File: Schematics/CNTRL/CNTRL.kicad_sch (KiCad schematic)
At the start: 128 parts, among them J1 SWD, J10 Y+, J11 Y-, J12 693071020811, J13 3.3V, J14 NAV I2C, J15 I2C, J16 USART, J17 PYRO1_OSTTE020104, J18 PYRO3_OSTTE020104, J19 USB_A_TE_292303-7_Horizontal, J2 CONSMA001-SMD-G-T, J20 PYRO2_OSTTE020104, J21 PYRO4_OSTTE020104, J3 3S LiPo, J4 F4, J5 F3, J6 F2, J7 F1, J8 X+, J9 X-, Q1 BUK9832-55A_CUX, Q2 BUK9832-55A_CUX, Q3 BUK9832-55A_CUX, Q4 BUK9832-55A_CUX, Q5 MMBT2222A-TP, SW1 OS102011MS2QN1, SW2 Omron_B3F-10xx, U1 STM32405RGT6, U2 RFM95W-915S2, U3 TPS2117DRLR, U4 TPS563200, U5 AMS1117-3.3, U6 AMS1117-5.0, U7 W25Q128JVSIQ, U8 USBLC6-2SC6, Y1 12MHz_ECS-120-18-33-JGN-TR3, Y2 32.768KHz_SC32S-7PF20PPM

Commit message: navig board pcb and schematic along with cntrl board edits
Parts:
- removed R11: 100K, Resistor_SMD:R_0603_1608Metric, symbol Device:R
- removed R22, R23, R36, R37: 10K, Resistor_SMD:R_0603_1608Metric, symbol Device:R
- removed R27, R28, R40, R41: 3.7K, Resistor_SMD:R_0603_1608Metric, symbol Device:R
- removed SW1: OS102011MS2QN1, External:SW_OS102011MS2QN1, symbol Switch:SW_SPDT
- added SW1: Omron_B3F-10xx, Button_Switch_THT:SW_TH_Tactile_Omron_B3F-10xx, symbol Switch:SW_Push
- J14: value NAV I2C -> NAVIG I2C
- R12: value 100K -> 10K
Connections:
- net +3.3V: now also SW1.2
- net BOOT0: now also SW1.1
- net GND: now also R1.2
- net PYRO_1_SENSE: no longer names the net of U1.9 (PC1)
- net PYRO_2_SENSE: no longer names the net of U1.11 (PC3)
- net PYRO_3_SENSE: no longer names the net of U1.26 (PB0)
- net PYRO_4_SENSE: no longer names the net of U1.28 (PB2)
- no-connect marks 10 -> 14

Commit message: NAVIG v1 fixes and some experimental CNTRL updates for v2
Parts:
- removed C24, C26: 10uF, Capacitor_SMD:C_0603_1608Metric, symbol Device:C
- removed Q5: MMBT2222A-TP, Package_TO_SOT_SMD:SOT-23, symbol Simulation_SPICE:NPN
- removed U6: AMS1117-5.0, Package_TO_SOT_SMD:SOT-223-3_TabPin2, symbol Regulator_Linear:AMS1117-5.0
- added Q5: BUK9832-55A_CUX, BUK9832-55A_CUX:TRANS_BUK9832-55A_CUX, symbol BUK9832-55A_CUX:BUK9832-55A_CUX
- added R11, R22, R23, R27, R36, R40, R42, R44: 10K, Resistor_SMD:R_0603_1608Metric, symbol Device:R
- added R28, R37, R41, R43: 68, Resistor_SMD:R_0603_1608Metric, symbol Device:R
- added U10, U11, U6, U9: TLP293GB-TPL_E, External:SO4_TOS, symbol TLP293:TLP293GB-TPL_E
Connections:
- net +3.3V: now also R11.2, R22.1, R23.2, R27.2, R28.2, R36.1, R37.2, R40.1, R41.2, R42.1, R43.2, R44.1
- net BUCK_+5V: now also C22.1, L2.2, R13.1
- net GND: now also Q5.3, U10.3, U11.3, U6.3, U9.3
- net SPI2_CSB: now also R22.2
- net SPI2_MISO: now also R27.1
- net SPI3_CSB: now also R11.1
- net SPI3_MISO: now also R23.1
- net at Q4.2, Q4.4, R30.1: now also U11.2
- net at Q3.2, Q3.4, R29.1: now also U9.2
- net at Q2.2, Q2.4, R19.1: now also U10.2
- net at Q1.2, Q1.4, R18.1: now also U6.2
- net at BZ1.2 (+): now also Q5.2, Q5.4
- net at R31.1: now also Q5.1
- net PYRO_2_SENSE: now reaches U1.11 (PC3)
- net PYRO_2_SENSE: now also R40.2, U9.4
- net PYRO_3_SENSE: now reaches U1.26 (PB0)
- net PYRO_3_SENSE: now also R44.2, U10.4
- net PYRO_4_SENSE: now reaches U1.28 (PB2)
- net PYRO_4_SENSE: now also R42.2, U11.4
- net PYRO_1_SENSE: now reaches U1.9 (PC1)
- net PYRO_1_SENSE: now also R36.2, U6.4
- new net: R28.1, U6.1
- new net: R37.1, U9.1
- new net: R41.1, U11.1
- new net: R43.1, U10.1
- no-connect marks 14 -> 10
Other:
- moved on the sheet: J17, J18, J20, J21, Q1, Q2, Q3, Q4, R18, R19, R20, R21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

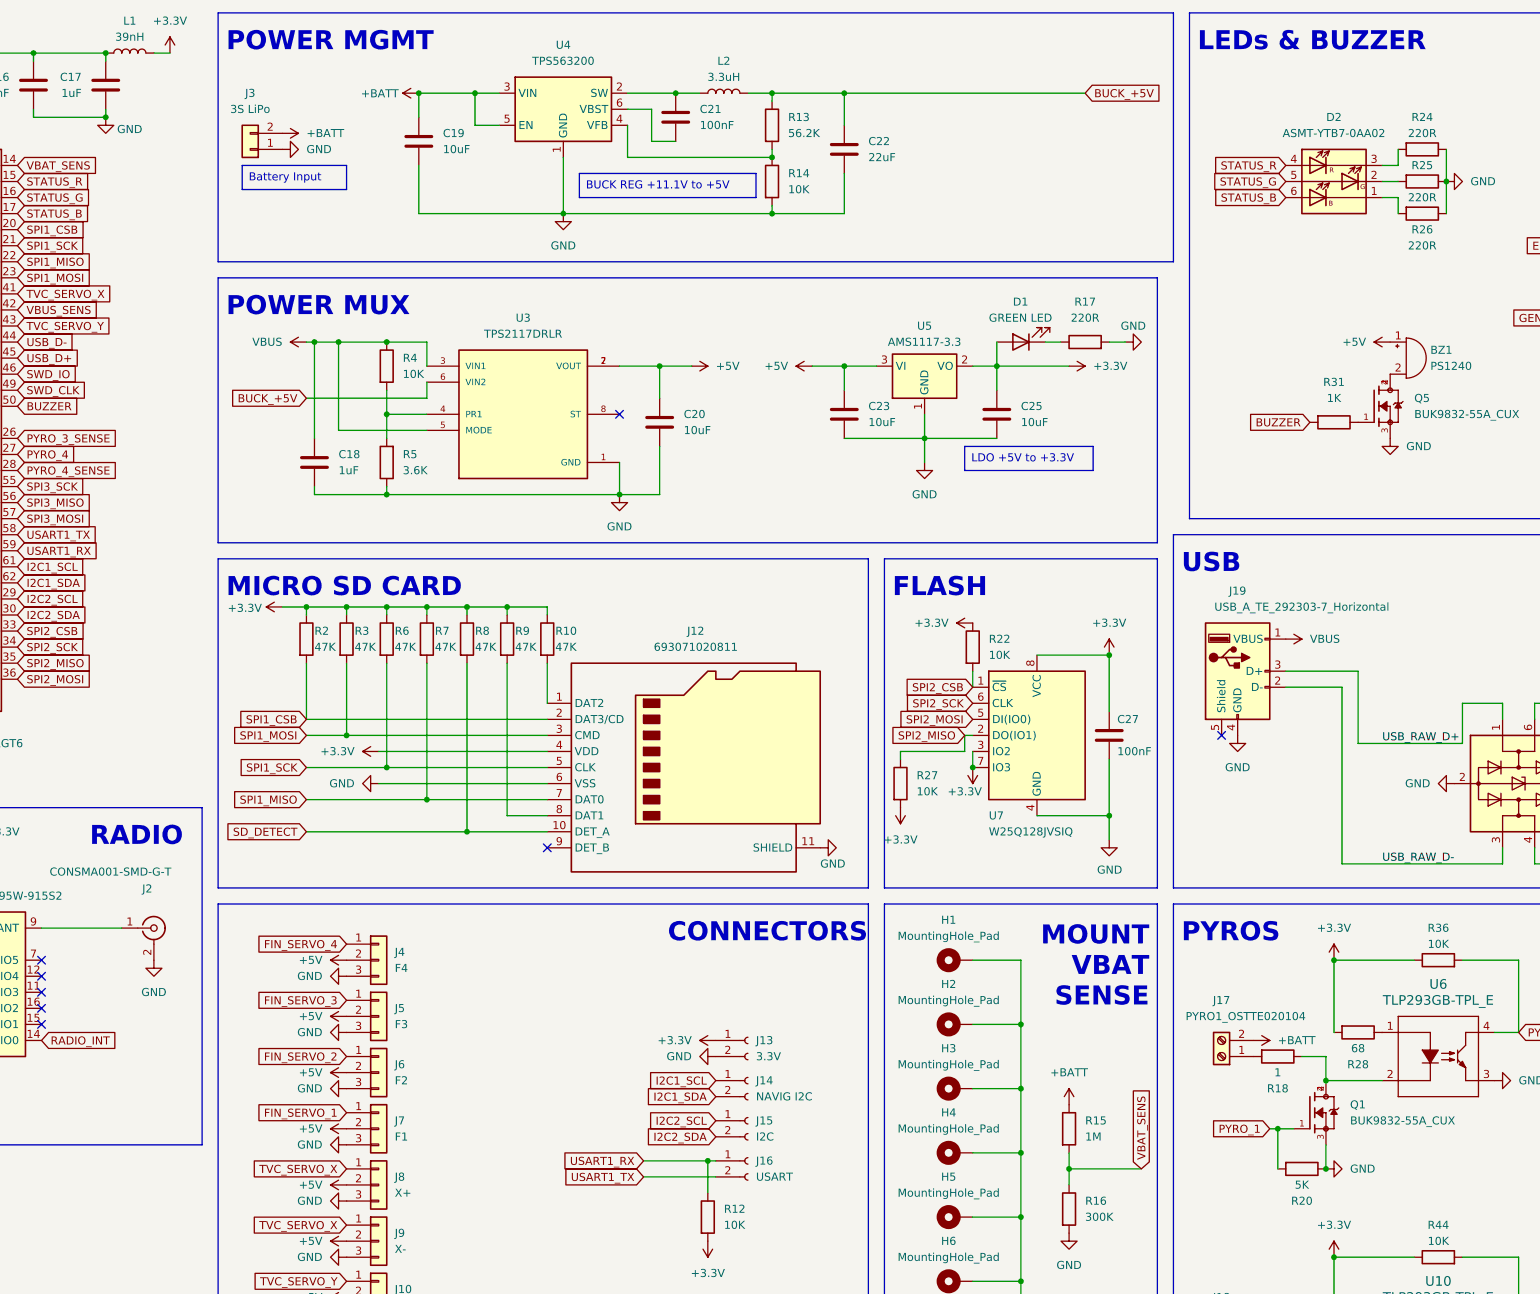
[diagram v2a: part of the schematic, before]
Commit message: initial coding/integration
i2c slave done (kinda doesnt work)
bno055 done (untested)
bmp390 done (untested)
neom9n not done
w25q128jv done (untested)
sd card/fatfs not done
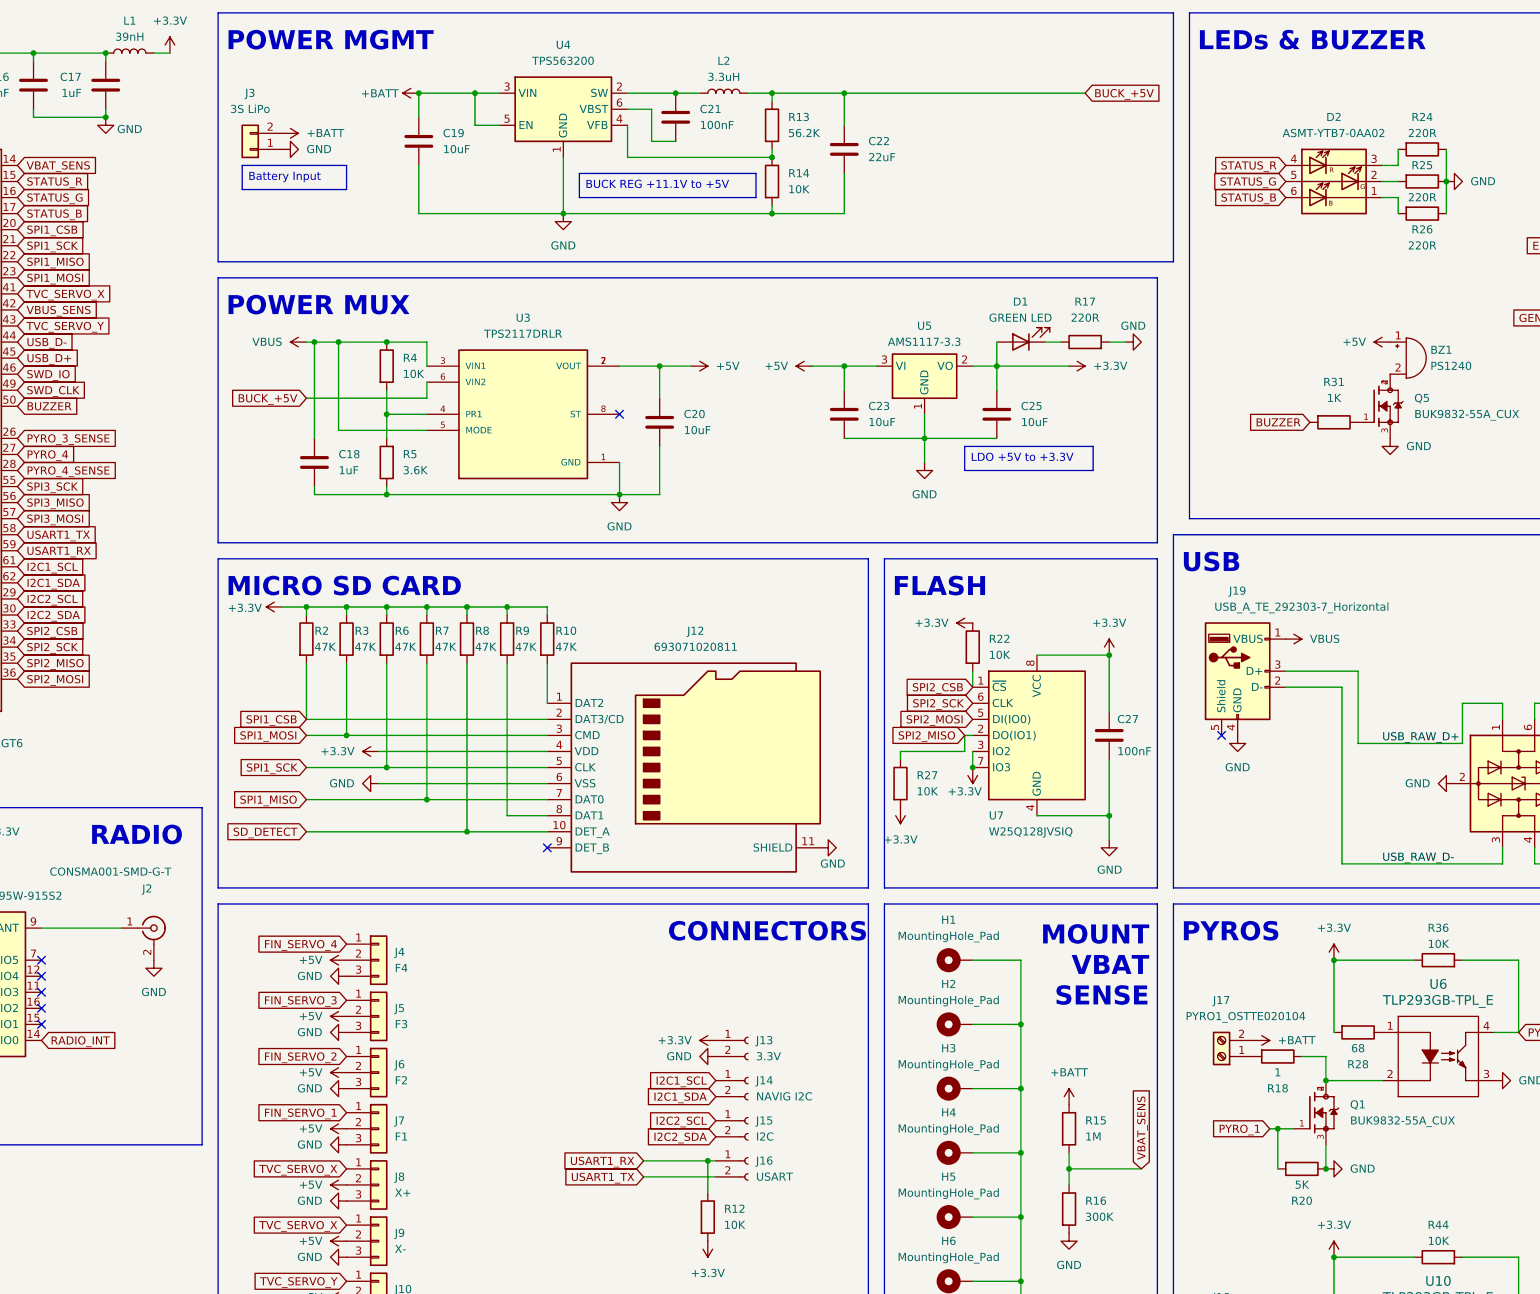
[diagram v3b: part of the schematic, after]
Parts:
- Y2: value 32.768KHz_SC32S-7PF20PPM -> 32.768KHz_SC32S-7PF20PPM
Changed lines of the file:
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@@
-(kicad_sch (version 20230121) (generator eeschema)
-  (paper "A2")
-  (title_block
-    (title "NAVION CNTRL BOARD SCHEMATIC")
-    (date "2024-08-04")
-    (company "NAVION")
-  )
+(kicad_sch
+	(version 20250114)
+	(generator "eeschema")
+	(generator_version "9.0")
+	(paper "A2")
+	(title_block
+		(title "NAVION CNTRL BOARD SCHEMATIC")
+		(date "2024-08-04")
+		(company "NAVION")
+	)

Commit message: CNTRL fixes towards v1.1
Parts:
- removed R28: 68, Resistor_SMD:R_0603_1608Metric, symbol Device:R
- removed R36: 10K, Resistor_SMD:R_0603_1608Metric, symbol Device:R
- removed U10, U11, U6, U9: TLP293GB-TPL_E, External:SO4_TOS, symbol TLP293:TLP293GB-TPL_E
- added J22: Reset Jumper, Connector_PinHeader_2.54mm:PinHeader_1x02_P2.54mm_Vertical, symbol Connector_Generic:Conn_01x02
- added R45: 10K, Resistor_SMD:R_0603_1608Metric, symbol Device:R
- added R46: 3.7K, Resistor_SMD:R_0603_1608Metric, symbol Device:R
- R34: value 82K -> 10K
- R35: value 33K -> 4.7K
- R37, R41, R43: value 68 -> 10K
- R40, R42, R44: value 10K -> 3.7K
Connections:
- net +3.3V: no longer R37.2, R40.1, R41.2, R42.1, R43.2, R44.1
- net GND: now also R40.2, R42.2, R44.2, R46.2
- net PYRO_1_SENSE: now also R45.2, R46.1
- net PYRO_2_SENSE: now also R37.2, R40.1; no longer R40.2
- net PYRO_3_SENSE: now also R41.2, R42.1; no longer R44.2
- net PYRO_4_SENSE: now also R43.2, R44.1; no longer R42.2
- net SWD_NRST: now also J22.1 (Pin_1); no longer SW2.1
- net at Q1.2, Q1.4, R18.1: now also R45.1
- net at Q4.2, Q4.4, R30.1: now also R43.1
- net at R37.1: now also Q3.2, Q3.4, R29.1
- net at Q2.2, Q2.4, R19.1: now also R41.1
- new net: J22.2 (Pin_2), SW2.1
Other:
- moved on the sheet: D3, D4, J18, J20, J21, Q2, Q3, Q4, R1, R19, R21, R29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

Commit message: CNTRL v1.1 fixes
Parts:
- removed J11: Y-, Connector_PinHeader_2.54mm:PinHeader_1x03_P2.54mm_Vertical, symbol Connector_Generic:Conn_01x03
- removed J19: USB_A_TE_292303-7_Horizontal, Connector_USB:USB_A_TE_292303-7_Horizontal, symbol Connector:USB_A
- removed J4: F4, Connector_PinHeader_2.54mm:PinHeader_1x03_P2.54mm_Vertical, symbol Connector_Generic:Conn_01x03
- removed J5: F3, Connector_PinHeader_2.54mm:PinHeader_1x03_P2.54mm_Vertical, symbol Connector_Generic:Conn_01x03
- removed J6: F2, Connector_PinHeader_2.54mm:PinHeader_1x03_P2.54mm_Vertical, symbol Connector_Generic:Conn_01x03
- removed J7: F1, Connector_PinHeader_2.54mm:PinHeader_1x03_P2.54mm_Vertical, symbol Connector_Generic:Conn_01x03
- removed J9: X-, Connector_PinHeader_2.54mm:PinHeader_1x03_P2.54mm_Vertical, symbol Connector_Generic:Conn_01x03
- added C24, C26, C31, C32: 100nF, Capacitor_SMD:C_0603_1608Metric, symbol Device:C
- added C29, C30: 470uF, Capacitor_THT:CP_Radial_D6.3mm_P2.50mm, symbol Device:C
- added J19: 3.3V, Connector_JST:JST_XH_B2B-XH-A_1x02_P2.50mm_Vertical, symbol Connector:Conn_01x02_Socket
- added J23: USB_C_Receptacle_USB2.0, Connector_USB:USB_C_Receptacle_GCT_USB4105-xx-A_16P_TopMnt_Horizontal, symbol Connector:USB_C_Receptacle_USB2.0
- added J24: 5V, Connector_JST:JST_XH_B2B-XH-A_1x02_P2.50mm_Vertical, symbol Connector:Conn_01x02_Socket
- added J5: GPIO 1-2, TerminalBlock_Phoenix:TerminalBlock_Phoenix_MPT-0,5-2-2.54_1x02_P2.54mm_Horizontal, symbol Connector:Conn_01x02_Socket
- added J6: GPIO 3-4, TerminalBlock_Phoenix:TerminalBlock_Phoenix_MPT-0,5-2-2.54_1x02_P2.54mm_Horizontal, symbol Connector:Conn_01x02_Socket
- added R28: 10K, Resistor_SMD:R_0603_1608Metric, symbol Device:R
- added R36, R47: 5.1K, Resistor_SMD:R_0603_1608Metric, symbol Device:R
- J10: value Y+ -> Y; footprint Connector_PinHeader_2.54mm:PinHeader_1x03_P2.54mm_Vertical -> TerminalBlock_Phoenix:TerminalBlock_Phoenix_MPT-0,5-3-2.54_1x03_P2.54mm_Horizontal
- J15: value I2C -> ESP32 I2C
- J8: value X+ -> X; footprint Connector_PinHeader_2.54mm:PinHeader_1x03_P2.54mm_Vertical -> TerminalBlock_Phoenix:TerminalBlock_Phoenix_MPT-0,5-3-2.54_1x03_P2.54mm_Horizontal
- Q1, Q2, Q3, Q4, Q5: footprint BUK9832-55A_CUX:TRANS_BUK9832-55A_CUX -> External:TRANS_BUK9832-55A_CUX
- U7: footprint Package_SO:SOIC-8_5.23x5.23mm_P1.27mm -> Package_SO:SOIC-8_5.3x5.3mm_P1.27mm
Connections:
- net +3.3V: now also J19.1 (Pin_1)
- net +5V: now also C29.2, C30.2, C31.2, C32.2, J24.1 (Pin_1)
- net +BATT: now also C26.1, R28.1; no longer U4.5 (EN)
- net BUCK_+5V: now also C18.1, R4.1, U3.3 (VIN1), U3.5 (MODE); no longer U3.6 (VIN2)
- net GND: now also C24.1, C26.2, C29.1, C30.1, C31.1, C32.1, J19.2 (Pin_2), J23.A1 (GND), J23.A12 (GND), J23.B1 (GND), J23.B12 (GND), J24.2 (Pin_2), R36.2, R47.2
- net USB_RAW_D+: now also J23.A6 (D+), J23.B6 (D+)
- net USB_RAW_D-: now also J23.A7 (D-), J23.B7 (D-)
- net VBAT_SENS: now also C24.2
- net VBUS: now also U3.6 (VIN2), J23.A4 (VBUS), J23.A9 (VBUS), J23.B4 (VBUS), J23.B9 (VBUS); no longer C18.1, R4.1, U3.3 (VIN1), U3.5 (MODE)
- net FIN_SERVO_1 renamed IO1
- net IO1: now also J5.1 (Pin_1)
- net FIN_SERVO_2 renamed IO2
- net IO2: now also J5.2 (Pin_2)
- net FIN_SERVO_3 renamed IO3
- net IO3: now also J6.1 (Pin_1)
- net FIN_SERVO_4 renamed IO4
- net IO4: now also J6.2 (Pin_2)
- new net: R28.2, U4.5 (EN)
- new net: J23.B5 (CC2), R47.1
- new net: J23.A5 (CC1), R36.1
- no-connect marks 10 -> 12
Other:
- moved on the sheet: C19, C21, C22, C28, J10, J13, J14, J15, J16, J8, L2, R12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

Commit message: final CNTRL v1.1
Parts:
- added R48, R49, R50, R51: 5K, Resistor_SMD:R_0603_1608Metric, symbol Device:R
- R37, R41, R43, R45: value 10K -> 5K
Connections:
- net PYRO_1_SENSE: now also R48.2; no longer R45.2
- net PYRO_2_SENSE: now also R51.2; no longer R37.2
- net PYRO_3_SENSE: now also R49.2; no longer R41.2
- net PYRO_4_SENSE: now also R50.2; no longer R43.2
- new net: R37.2, R51.1
- new net: R43.2, R50.1
- new net: R41.2, R49.1
- new net: R45.2, R48.1
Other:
- moved on the sheet: J20, J21, Q3, Q4, R29, R30, R32, R33, R37, R40, R42, R43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
